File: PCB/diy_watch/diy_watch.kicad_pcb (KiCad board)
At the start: 2 copper layers, 37 x 37 mm, 38 parts, among them J1 USB_B_Micro, SW1 SW_Push, U1 W25Q32JVSS, U2 DS3231MZ, U3 RP2040, U5 LTC4054ES5-4.2, U7 XC6210B332MR, Y1 12MHz_crystal

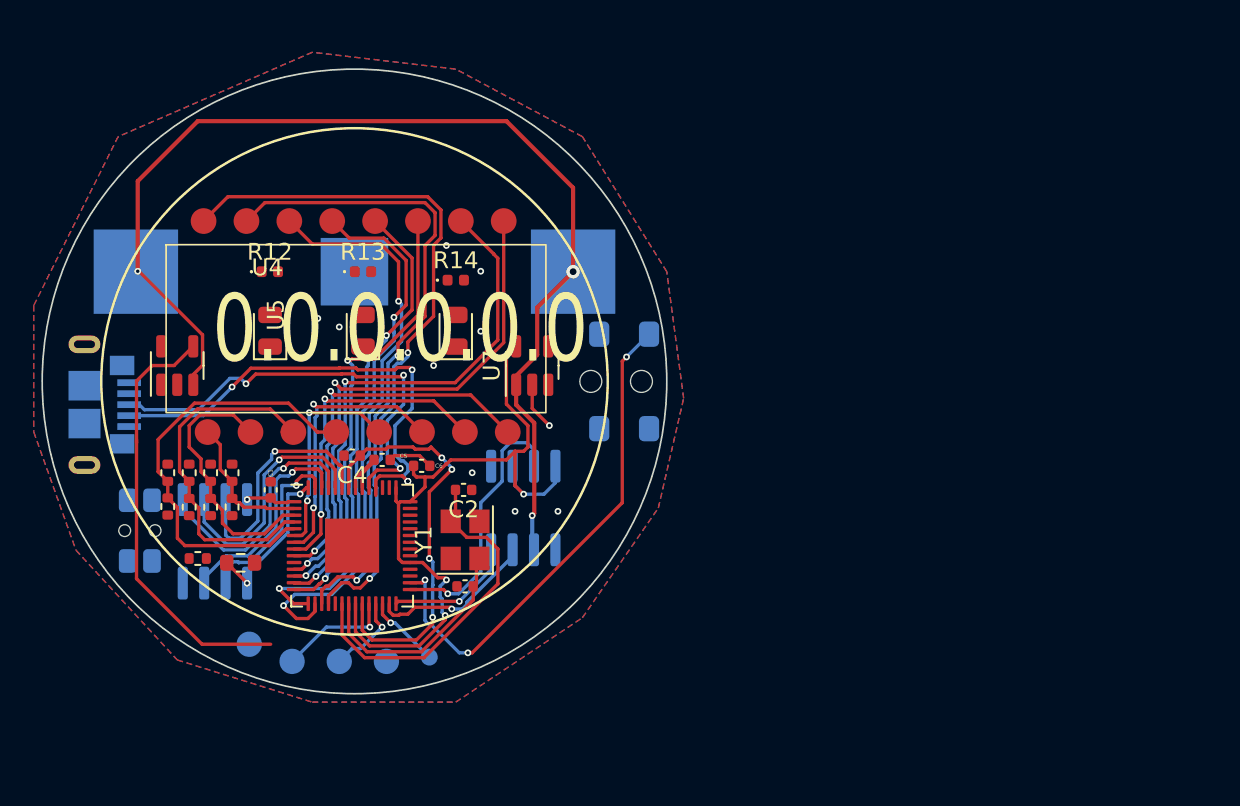
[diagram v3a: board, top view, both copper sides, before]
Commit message: Finished wiring, not started on DRC errors
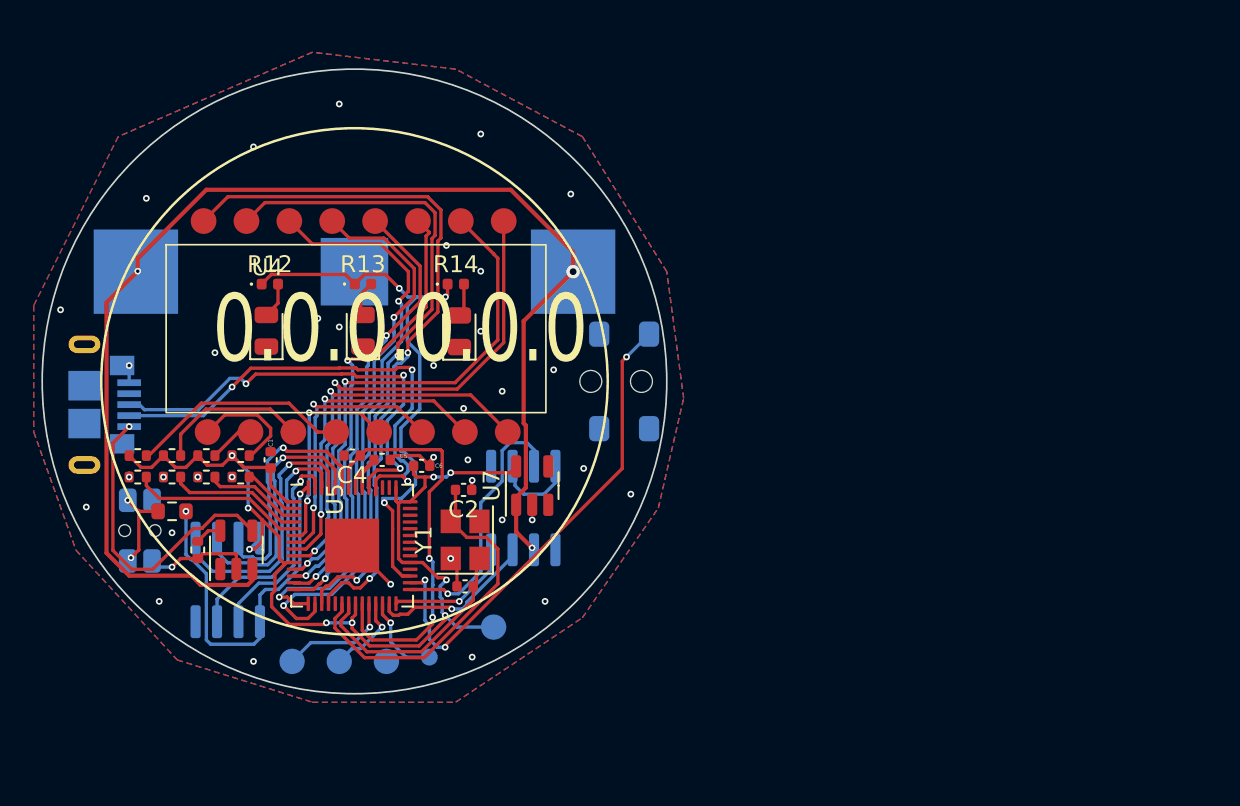
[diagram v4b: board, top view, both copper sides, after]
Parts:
- moved TP5 14.5 mm to (158.2, 114.6)
- moved U5 11.5 mm to (143.0, 110.0)
- moved U7 7.11 mm to (160.5, 106.2)
- moved R1 5.08 mm to (139.2, 107.7), turned to 0 degrees
- moved R10 2.49 mm to (137.2, 105.7), turned to 180 degrees
- moved U1 2.41 mm to (142.5, 111.8)
- moved R8 2.05 mm to (139.2, 105.7), turned to 180 degrees
- moved R9 2.05 mm to (137.2, 104.4), turned to 0 degrees
- moved R4 1.85 mm to (143.3, 105.7), turned to 180 degrees
- moved R6 1.80 mm to (141.2, 105.7), turned to 180 degrees
- moved C1 1.78 mm to (145.0, 104.6)
- moved R7 1.44 mm to (139.2, 104.4), turned to 0 degrees
- moved R3 1.14 mm to (143.3, 104.4), turned to 0 degrees
- moved R5 1.05 mm to (141.2, 104.4), turned to 0 degrees
- moved R12 0.73 mm to (145.0, 94.2)
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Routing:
- net /light_en: track 0.00 -> 33.4 mm, vias 0 -> 3
- net +3.3V: track 50.4 -> 72.9 mm, vias 4 -> 9
- net Net-(U1-~{CS}): track 9.34 -> 22.2 mm
- net GND: track 7.65 -> 18.8 mm, vias 10 -> 37
- net +BATT: track 66.2 -> 77.0 mm
- net +5V: track 25.7 -> 18.2 mm, vias 0 -> 1
- net /COM2: track 15.9 -> 8.46 mm
- net Net-(R1-Pad1): track 0.00 -> 5.02 mm, vias 0 -> 2
- net /COM3: track 22.0 -> 18.4 mm
- net /COM4: track 26.0 -> 23.6 mm
- net Net-(D2-A): track 0.00 -> 2.14 mm
- net Net-(D1-A): track 0.00 -> 2.11 mm
- net Net-(U1-IO2): track 12.6 -> 14.6 mm
- net Net-(D3-A): track 0.00 -> 1.97 mm
- net /COM1: track 8.45 -> 10.1 mm
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
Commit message: Added caps to regulator, Changed edge cut
Adding missing pullup on switch
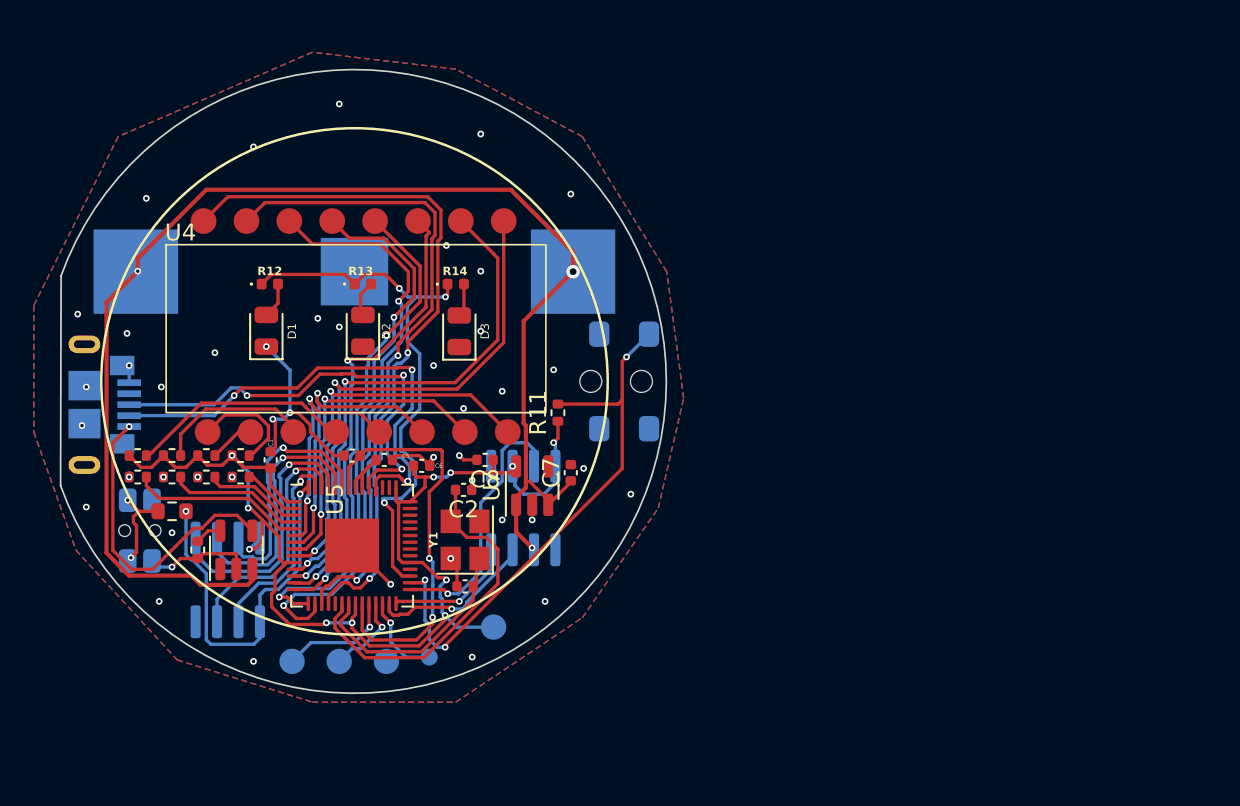
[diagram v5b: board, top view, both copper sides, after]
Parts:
- added C7: 1uF, Capacitor_SMD:C_0402_1005Metric, F.Cu at (162.8, 105.4)
- added C8: 1uF, Capacitor_SMD:C_0402_1005Metric, F.Cu at (157.7, 104.6)
- added R11: 100K, Resistor_SMD:R_0402_1005Metric, F.Cu at (162.1, 101.9)
- moved C5 0.13 mm to (151.8, 104.6)
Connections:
- U7 pad 3: unconnected-(U7-CE-Pad3) -> +BATT
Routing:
- net GND: track 18.8 -> 32.1 mm, vias 37 -> 44
- net +BATT: track 77.0 -> 81.0 mm
- net +3.3V: track 72.9 -> 76.8 mm, vias 9 -> 11
- net /light_sw: track 29.3 -> 33.2 mm
- net /A: track 12.5 -> 14.1 mm
- net /B: track 16.3 -> 17.3 mm
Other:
- board size 37 x 37 mm -> 35.9 x 36.9 mm

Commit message: Updated silkscreen names
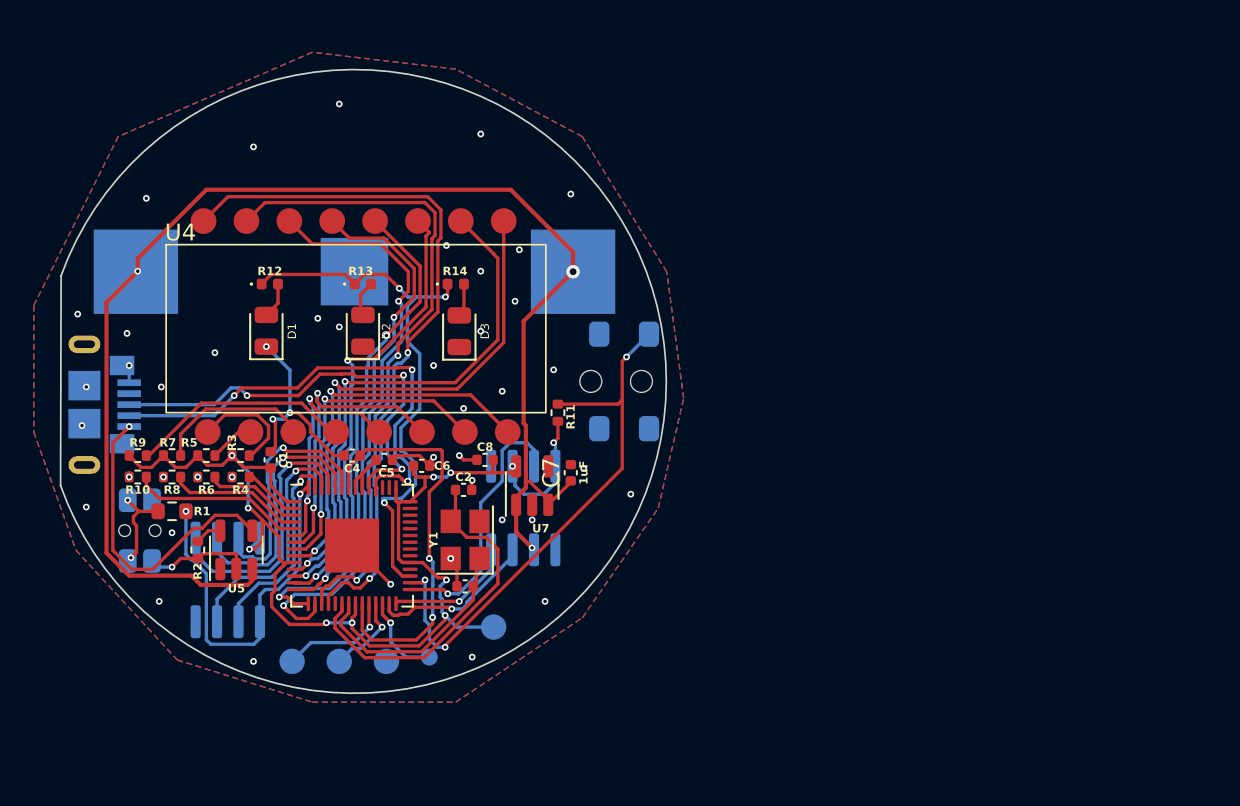
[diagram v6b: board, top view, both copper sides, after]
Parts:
- TP4: value TestPoint -> TP_Run
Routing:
- net GND: vias 44 -> 46

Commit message: Removed wires and Rearranged PCB layout to create more space
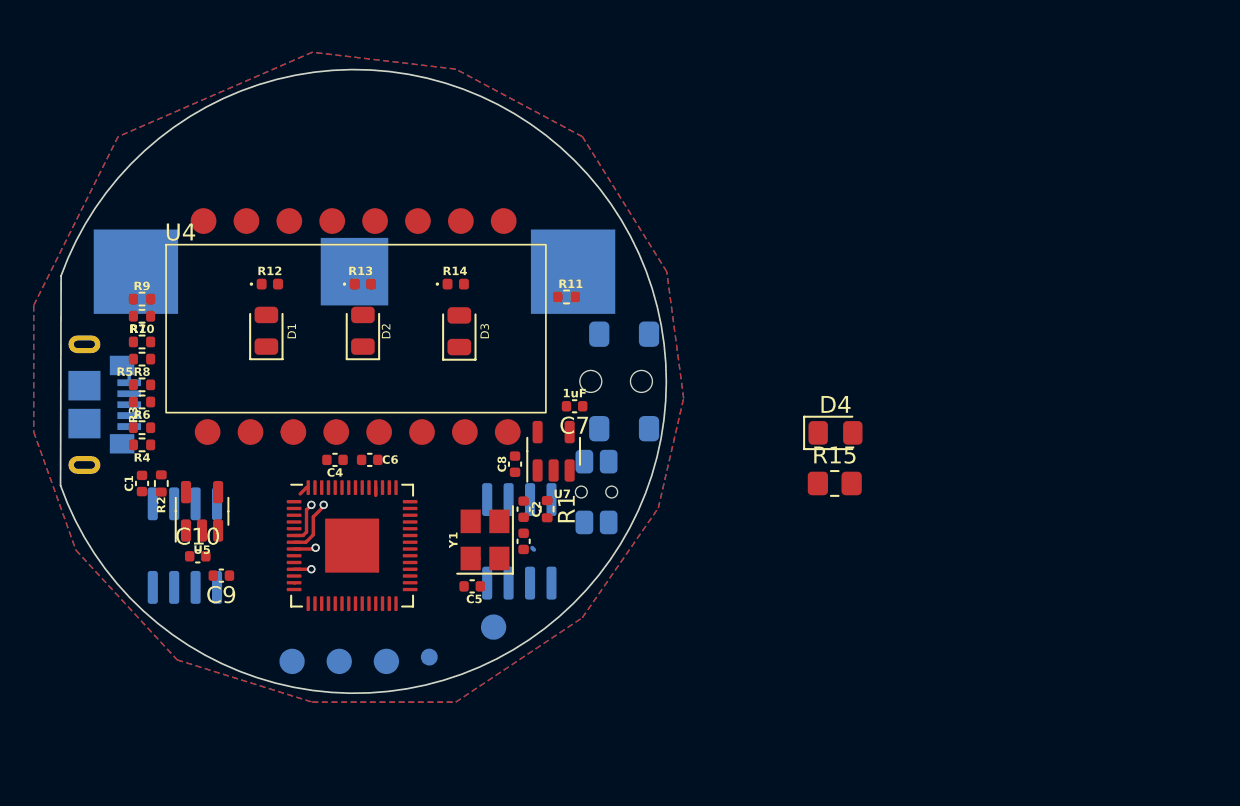
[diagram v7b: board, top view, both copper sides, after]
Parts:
- added C10: 1uf, Capacitor_SMD:C_0402_1005Metric, F.Cu at (140.7, 110.4)
- added C9: 1uF, Capacitor_SMD:C_0402_1005Metric, F.Cu at (142.1, 111.5)
- added D4: LED, LED_SMD:LED_0805_2012Metric_Pad1.15x1.40mm_HandSolder, F.Cu at (178.5, 103.0)
- added R15: 330, Resistor_SMD:R_0805_2012Metric_Pad1.20x1.40mm_HandSolder, F.Cu at (178.5, 106.0)
- R1: footprint Resistor_SMD:R_0603_1608Metric -> Resistor_SMD:R_0402_1005Metric
- R2: value R -> 25K
- moved SW1 27.1 mm to (164.3, 106.6), turned to -90 degrees
- moved R1 22.2 mm to (161.4, 107.6), turned to -90 degrees
- moved R10 9.53 mm to (137.4, 96.1)
- moved R9 9.27 mm to (137.4, 95.1)
- moved C5 9.12 mm to (157.0, 112.1)
- moved C1 7.75 mm to (137.4, 106.0), turned to -90 degrees
- moved R8 7.21 mm to (137.4, 98.7)
- moved R7 6.96 mm to (137.4, 97.7)
- moved R11 6.88 mm to (162.6, 95.0), turned to 180 degrees
- moved R4 6.14 mm to (137.4, 103.8)
- moved R3 6.07 mm to (137.4, 102.7)
- moved R6 5.85 mm to (137.4, 101.2)
- moved R5 5.66 mm to (137.4, 100.2)
- moved R2 4.49 mm to (138.6, 106.0)
- moved C3 4.38 mm to (160.0, 109.5), turned to -90 degrees
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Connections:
- U5 pad 1: unconnected-(U5-~{CHRG}-Pad1) -> Net-(U5-~{CHRG})
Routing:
- net +BATT: track 81.0 -> 0.15 mm, vias 3 -> 0
- net +3.3V: track 76.8 -> 0.00 mm, vias 11 -> 0
- net /L: track 42.4 -> 0.00 mm, vias 2 -> 0
- net /K: track 39.1 -> 0.00 mm, vias 2 -> 0
- net /J: track 35.5 -> 0.00 mm, vias 2 -> 0
- net /light_en: track 33.4 -> 0.00 mm, vias 3 -> 0
- net /light_sw: track 33.2 -> 0.11 mm, vias 3 -> 0
- net /I: track 32.2 -> 0.00 mm, vias 2 -> 0
- net /F: track 31.5 -> 0.00 mm, vias 2 -> 0
- net /E: track 31.3 -> 1.03 mm, vias 2 -> 1
- net GND: track 32.1 -> 3.55 mm, vias 46 -> 0
- net /usb_D-: track 28.6 -> 0.46 mm, vias 4 -> 0
- net /H: track 26.8 -> 0.00 mm, vias 2 -> 0
- net /G: track 26.8 -> 0.04 mm, vias 2 -> 0
- net /usb_D+: track 26.5 -> 0.00 mm, vias 3 -> 0
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
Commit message: Changed charging chip and flash chip, rearranged parts
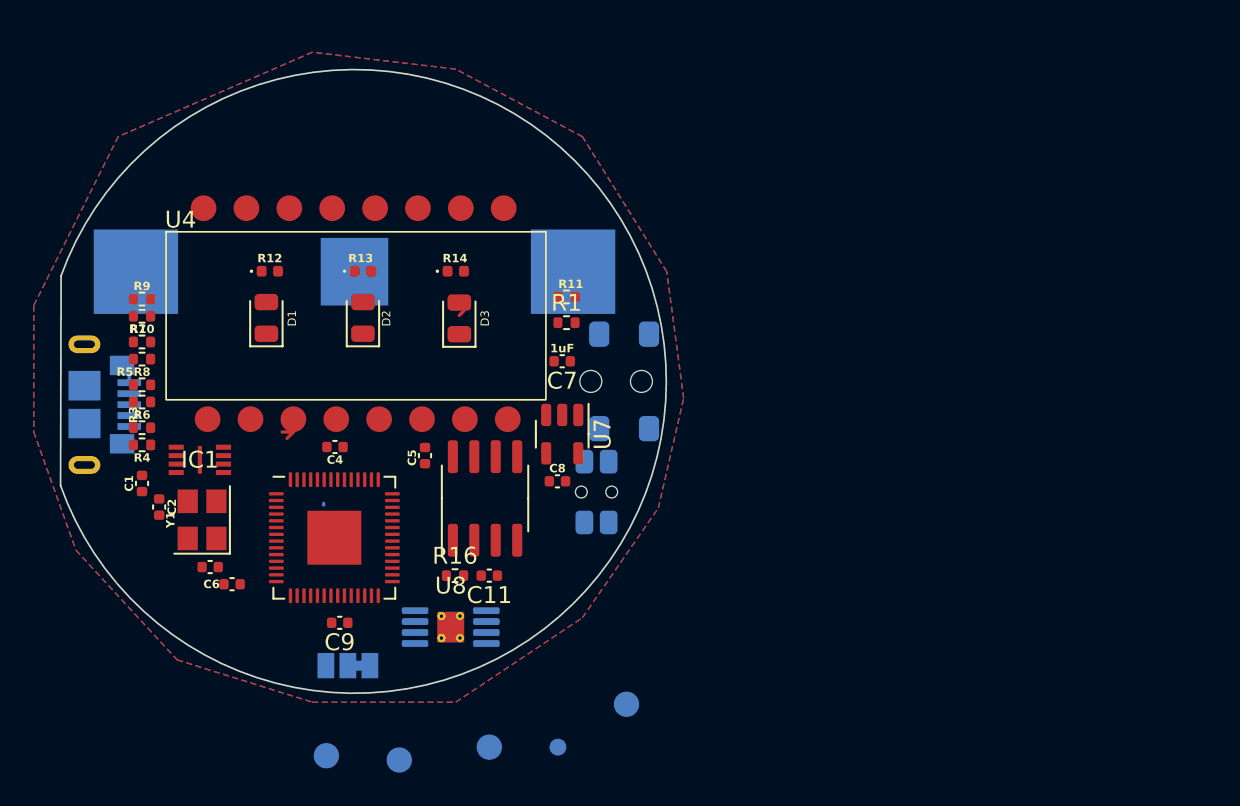
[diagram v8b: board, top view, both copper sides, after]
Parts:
- removed C10: 1uf, Capacitor_SMD:C_0402_1005Metric
- removed D4: LED, LED_SMD:LED_0805_2012Metric_Pad1.15x1.40mm_HandSolder
- removed R15: 330, Resistor_SMD:R_0805_2012Metric_Pad1.20x1.40mm_HandSolder
- removed R2: 25K, Resistor_SMD:R_0402_1005Metric
- removed U1: W25Q32JVSS, Package_SO:SOIC-8_3.9x4.9mm_P1.27mm
- removed U5: LTC4054ES5-4.2, Package_TO_SOT_SMD:TSOT-23-5
- added C11: 1uf, Capacitor_SMD:C_0402_1005Metric, F.Cu at (158.0, 111.5)
- added IC1: W25Q16JVUXIQ, DIY_Watch_lib:SON50P300X200X60-9N, F.Cu at (140.8, 104.6)
- added JP1: SolderJumper_3_Bridged12, Jumper:SolderJumper-3_P1.3mm_Bridged12_Pad1.0x1.5mm, B.Cu at (149.6, 116.8)
- added R16: 162, Resistor_SMD:R_0402_1005Metric, F.Cu at (156.0, 111.5)
- added U8: LTC4071EMS8E_PBF, Package_SO:MSOP-8-1EP_3x3mm_P0.65mm_EP1.5x1.8mm_ThermalVias, B.Cu at (155.7, 114.6)
- U2: moved to F.Cu
- moved C2 21.6 mm to (138.4, 107.4)
- moved C3 18.6 mm to (141.4, 111.0), turned to 0 degrees
- moved Y1 16.8 mm to (141.0, 108.2)
- moved R1 11.1 mm to (162.6, 96.5), turned to 0 degrees
- moved C6 11.0 mm to (142.7, 112.0), turned to 180 degrees
- moved TP4 9.30 mm to (162.1, 121.7)
- moved TP5 9.11 mm to (166.1, 119.1)
- moved C5 8.24 mm to (154.2, 104.4), turned to -90 degrees
- moved TP2 7.94 mm to (158.0, 121.7)
- moved C9 7.55 mm to (149.1, 114.3)
- moved TP3 6.84 mm to (152.7, 122.4)
- moved TP1 5.95 mm to (148.3, 122.2)
- moved U2 3.25 mm to (157.7, 106.9), turned to 90 degrees
- moved C7 2.77 mm to (162.3, 98.8)
- moved C8 2.71 mm to (162.0, 105.9), turned to 180 degrees
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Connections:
- BT1 pad 1: +BATT -> Net-(BT1-+)
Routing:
- net /B: track 3.44 -> 0.00 mm, vias 1 -> 0
- net /A: track 2.55 -> 0.00 mm, vias 1 -> 0
- net GND: track 3.55 -> 1.19 mm
- net /C: track 1.31 -> 0.00 mm, vias 1 -> 0
- net /E: track 1.03 -> 0.00 mm, vias 1 -> 0
- net Net-(IC1-~{CS}): track 0.64 -> 0.00 mm
